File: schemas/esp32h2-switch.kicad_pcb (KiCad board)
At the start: 2 copper layers, 81.3 x 58.4 mm, 21 parts, among them J1 Screw_Terminal_01x02, J2 Screw_Terminal_01x02, J3 Conn_01x15, J4 Conn_01x15, K1 SPDT, 5V 72R, 10A 250VAC, Q1 NPN, 40V, 500mA, U1 LM1117MP-3.3

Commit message: Fix nets due to checks
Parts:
- turned F1 to 0 degrees
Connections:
- F1 pad 1: L -> L_IN
- F1 pad 2: L -> /L
- J1 pad 1: L -> L_IN
- J2 pad 1: L -> /L_OUT
- K1 pad 11: L -> L_IN
- K1 pad 14: L -> /L_OUT
- PS1 pad 1: L -> /L
- RV1 pad 1: L -> /L
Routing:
- net L: track 73.9 -> 0.00 mm
- net L_IN: track 0.00 -> 40.1 mm
- net /L_OUT: track 0.00 -> 17.3 mm
- net /L: track 0.00 -> 16.5 mm
- net Net-(J3-Pin_9): track 66.8 -> 67.3 mm
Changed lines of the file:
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@@
 	(net 5 "/RELAY_COIL")
 	(net 6 "/LED_RELAY")
-	(net 7 "L")
+	(net 7 "L_IN")
 	(net 8 "unconnected-(J3-Pin_8-Pad8)")
 	(net 9 "/RELAY_CTRL")
@@
 	(net 37 "Net-(Q1-B)")
 	(net 38 "N")
+	(net 39 "/L")
+	(net 40 "/L_OUT")
 	(footprint "TerminalBlock_Phoenix:TerminalBlock_Phoenix_MKDS-1,5-2-5.08_1x02_P5.08mm_Horizontal"
 		(layer "F.Cu")
@@
 			(remove_unused_layers no)
 			(roundrect_rratio 0.096154)
-			(net 7 "L")
+			(net 40 "/L_OUT")
 			(pinfunction "Pin_1")
 			(pintype "passive")
@@
 			(layers "*.Cu" "*.Mask")
 			(remove_unused_layers no)
-			(net 7 "L")
+			(net 39 "/L")
 			(pinfunction "AC/L")
 			(pintype "power_in")
@@
 			(remove_unused_layers no)
 			(roundrect_rratio 0.096154)
-			(net 7 "L")
+			(net 7 "L_IN")
 			(pinfunction "Pin_1")
 			(pintype "passive")
@@
 		(tags "LED")
 		(property "Reference" "D1"
-			(at -0.635 -1.987701 180)
+			(at -0.635 -2.54 180)
 			(layer "F.SilkS")
 			(effects
@@
 	(footprint "Sivakov_FuseHolders_THT:FuseHolder_THT_5x20mm_PTF76_RM15mm"
 		(layer "F.Cu")
-		(at 57.15 62.23 180)
+		(at 57.15 62.23)
 		(property "Reference" "F1"
 			(at 0 0 0)
@@
 		(attr through_hole)
 		(fp_line
-			(start 12.3 4.8)
-			(end -12.3 4.8)
+			(start -12.3 -4.8)
+			(end 12.3 -4.8)
 			(stroke
 				(width 0.2)
@@
 		)
 		(fp_line
-			(start 12.3 -4.8)
-			(end 12.3 4.8)
+			(start -12.3 4.8)
+			(end -12.3 -4.8)
 			(stroke
 				(width 0.2)
@@
 		)
 		(fp_line
-			(start -12.3 4.8)
-			(end -12.3 -4.8)
+			(start 12.3 -4.8)
+			(end 12.3 4.8)
 			(stroke
 				(width 0.2)
@@
 		)
 		(fp_line
-			(start -12.3 -4.8)
-			(end 12.3 -4.8)
+			(start 12.3 4.8)
+			(end -12.3 4.8)
 			(stroke
 				(width 0.2)
@@
 		)
 		(fp_line
-			(start 12.5 5)
-			(end -12.5 5)
+			(start -12.5 -5)
+			(end 12.5 -5)
 			(stroke
 				(width 0.05)
-				(type default)
+				(type solid)
 			)
 			(layer "F.CrtYd")
 		)
 		(fp_line
-			(start 12.5 -5)
-			(end 12.5 5)
+			(start -12.5 5)
+			(end -12.5 -5)
 			(stroke
 				(width 0.05)
@@
 		)
 		(fp_line
-			(start -12.5 5)
-			(end -12.5 -5)
+			(start 12.5 -5)
+			(end 12.5 5)
 			(stroke
 				(width 0.05)
@@
 		)
 		(fp_line
-			(start -12.5 -5)
-			(end 12.5 -5)
+			(start 12.5 5)
+			(end -12.5 5)
 			(stroke
 				(width 0.05)
-				(type solid)
+				(type default)
 			)
 			(layer "F.CrtYd")
 		)
 		(fp_line
-			(start 12.2 4.7)
-			(end -12.2 4.7)
+			(start -12.2 -4.7)
+			(end 12.2 -4.7)
 			(stroke
 				(width 0.1)
@@
 		)
 		(fp_line
-			(start 12.2 -4.7)
-			(end 12.2 4.7)
+			(start -12.2 4.7)
+			(end -12.2 -4.7)
 			(stroke
 				(width 0.1)
@@
 		)
 		(fp_line
-			(start -12.2 4.7)
-			(end -12.2 -4.7)
+			(start 12.2 -4.7)
+			(end 12.2 4.7)
 			(stroke
 				(width 0.1)
@@
 		)
 		(fp_line
-			(start -12.2 -4.7)
-			(end 12.2 -4.7)
+			(start 12.2 4.7)
+			(end -12.2 4.7)
 			(stroke
 				(width 0.1)
@@
 		)
 		(pad "1" thru_hole circle
-			(at -7.5 0 180)
+			(at -7.5 0)
 			(size 2.5 2.5)
 			(drill 1.5)
 			(layers "*.Cu" "*.Mask")
 			(remove_unused_layers no)
-			(net 7 "L")
+			(net 7 "L_IN")
 			(pintype "passive")
 			(solder_mask_margin 0.102)
 		)
 		(pad "2" thru_hole circle
-			(at 7.5 0 180)
+			(at 7.5 0)
 			(size 2.25 2.25)
 			(drill 1.5)
 			(layers "*.Cu" "*.Mask")
 			(remove_unused_layers no)
-			(net 7 "L")
+			(net 39 "/L")
 			(pintype "passive")
 			(solder_mask_margin 0.102)
@@
 			(layers "*.Cu" "*.Mask")
 			(remove_unused_layers no)
-			(net 7 "L")
+			(net 39 "/L")
 			(pintype "passive")
 		)
@@
 		(tags "LED")
 		(property "Reference" "D3"
-			(at -0.635 -1.905 180)
+			(at -0.635 -2.54 180)
 			(layer "F.SilkS")
 			(effects
@@
 			(layers "*.Cu" "*.Mask")
 			(remove_unused_layers no)
-			(net 7 "L")
+			(net 7 "L_IN")
 			(pintype "passive")
 		)
@@
 			(layers "*.Cu" "*.Mask")
 			(remove_unused_layers no)
-			(net 7 "L")
+			(net 40 "/L_OUT")
 			(pintype "passive")
 		)
@@
 	)
 	(segment
-		(start 42.476571 73.66)
-		(end 47.86 79.043429)
-		(width 3)
-		(layer "B.Cu")
-		(net 7)
-	)
-	(segment
-		(start 57.277142 62.23)
-		(end 64.869 69.821858)
-		(width 3)
-		(layer "B.Cu")
-		(net 7)
-	)
-	(segment
-		(start 76.708 67.564)
-		(end 73.152 67.564)
-		(width 3)
-		(layer "B.Cu")
-		(net 7)
-	)
-	(segment
-		(start 47.86 79.043429)
-		(end 47.86 84.3245)
-		(width 3)
-		(layer "B.Cu")
-		(net 7)
-	)
-	(segment
-		(start 49.65 62.23)
-		(end 57.277142 62.23)
-		(width 3)
-		(layer "B.Cu")
-		(net 7)
-	)
-	(segment
 		(start 38.1 60.96)
 		(end 48.38 60.96)
@@
 	)
 	(segment
-		(start 73.152 67.564)
-		(end 71.12 69.596)
-		(width 3)
-		(layer "B.Cu")
-		(net 7)
-	)
-	(segment
-		(start 64.65 63.126)
-		(end 71.12 69.596)
-		(width 3)
-		(layer "B.Cu")
-		(net 7)
-	)
-	(segment
-		(start 64.869 69.821858)
-		(end 64.869 75.5155)
+		(start 64.811 75.5735)
+		(end 62.06 78.3245)
 		(width 3)
 		(layer "B.Cu")
@@
 	)
 	(segment
-		(start 64.65 62.23)
-		(end 64.65 63.126)
+		(start 49.65 62.23)
+		(end 57.277142 62.23)
 		(width 3)
 		(layer "B.Cu")
@@
 	)
 	(segment
-		(start 64.869 75.5155)
-		(end 62.06 78.3245)
+		(start 57.277142 62.23)
+		(end 64.811 69.763858)
 		(width 3)
 		(layer "B.Cu")
@@
 	)
 	(segment
-		(start 38.1 73.66)
-		(end 42.476571 73.66)
+		(start 64.811 69.763858)
+		(end 64.811 75.5735)
 		(width 3)
 		(layer "B.Cu")
@@
 	)
 	(segment
-		(start 65.914 113.156)
-		(end 88.9 90.17)
+		(start 42.545 109.22)
+		(end 46.99 113.665)
 		(width 0.25)
 		(layer "F.Cu")
@@
 	)
 	(segment
-		(start 42.545 109.22)
-		(end 46.481 113.156)
+		(start 65.405 113.665)
+		(end 88.9 90.17)
 		(width 0.25)
 		(layer "F.Cu")
@@
 	)
 	(segment
-		(start 46.481 113.156)
-		(end 65.914 113.156)
+		(start 46.99 113.665)
+		(end 65.405 113.665)
 		(width 0.25)
 		(layer "F.Cu")
@@
 	)
 	(segment
-		(start 36.195 109.22)
-		(end 40.582 113.607)
+		(start 41.275 114.3)
+		(end 67.31 114.3)
 		(width 0.25)
 		(layer "F.Cu")
@@
 	)
 	(segment
-		(start 40.582 113.607)
-		(end 68.003 113.607)
+		(start 67.31 114.3)
+		(end 91.44 90.17)
 		(width 0.25)
 		(layer "F.Cu")
@@
 	)
 	(segment
-		(start 68.003 113.607)
-		(end 91.44 90.17)
+		(start 36.195 109.22)
+		(end 41.275 114.3)
 		(width 0.25)
 		(layer "F.Cu")
@@
 		(net 38)
 	)
+	(segment
+		(start 64.65 62.23)
+		(end 64.65 63.126)
+		(width 3)
+		(layer "B.Cu")
+		(net 39)
+	)
+	(segment
+		(start 76.708 67.564)
+		(end 73.152 67.564)
+		(width 3)
+		(layer "B.Cu")
+		(net 39)
+	)
+	(segment
+		(start 64.65 63.126)
+		(end 71.12 69.596)
+		(width 3)
+		(layer "B.Cu")
+		(net 39)
+	)
+	(segment
+		(start 73.152 67.564)
+		(end 71.12 69.596)
+		(width 3)
+		(layer "B.Cu")
+		(net 39)
+	)
+	(segment
+		(start 42.476571 73.66)
+		(end 47.86 79.043429)
+		(width 3)
+		(layer "B.Cu")
+		(net 40)
+	)
+	(segment
+		(start 47.86 79.043429)
+		(end 47.86 84.3245)
+		(width 3)
+		(layer "B.Cu")
+		(net 40)
+	)
+	(segment
+		(start 38.1 73.66)
+		(end 42.476571 73.66)
+		(width 3)
+		(layer "B.Cu")
+		(net 40)
+	)
 	(zone
 		(net 3)
@@
 		(polygon
 			(pts
-				(xy 51.435 107.315) (xy 59.055 107.315) (xy 59.055 113.03) (xy 51.435 113.03)
-			)
-		)
-	)
-	(zone
-		(net 0)
-		(net_name "")
-		(layer "F.Cu")
-		(hatch edge 0.5)
-		(connect_pads yes
-			(clearance 0)
-		)
-		(min_thickness 0.25)
-		(filled_areas_thickness no)
-		(keepout
-			(tracks not_allowed)
-			(vias not_allowed)
-			(pads allowed)
-			(copperpour allowed)
-			(footprints allowed)
-		)
-		(placement
-			(enabled no)
-			(sheetname "/")
-		)
-		(fill
-			(thermal_gap 0.5)
-			(thermal_bridge_width 0.5)
-		)
-		(polygon
-			(pts
-				(xy 51.435 107.315) (xy 59.055 107.315) (xy 59.055 113.03) (xy 51.435 113.03)
+				(xy 51.435 106.045) (xy 59.055 106.045) (xy 59.055 113.03) (xy 51.435 113.03)
 			)
 		)

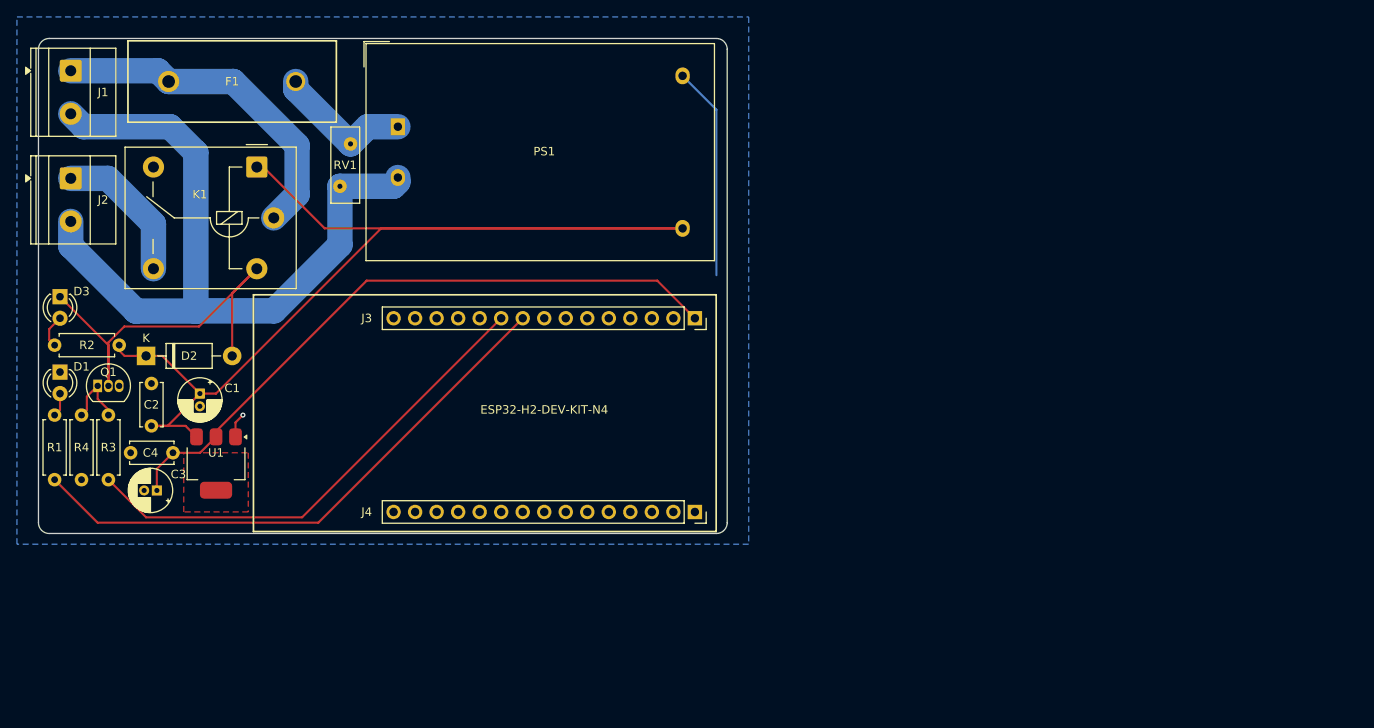
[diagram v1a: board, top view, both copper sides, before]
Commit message: Better arragement components + more copper fields
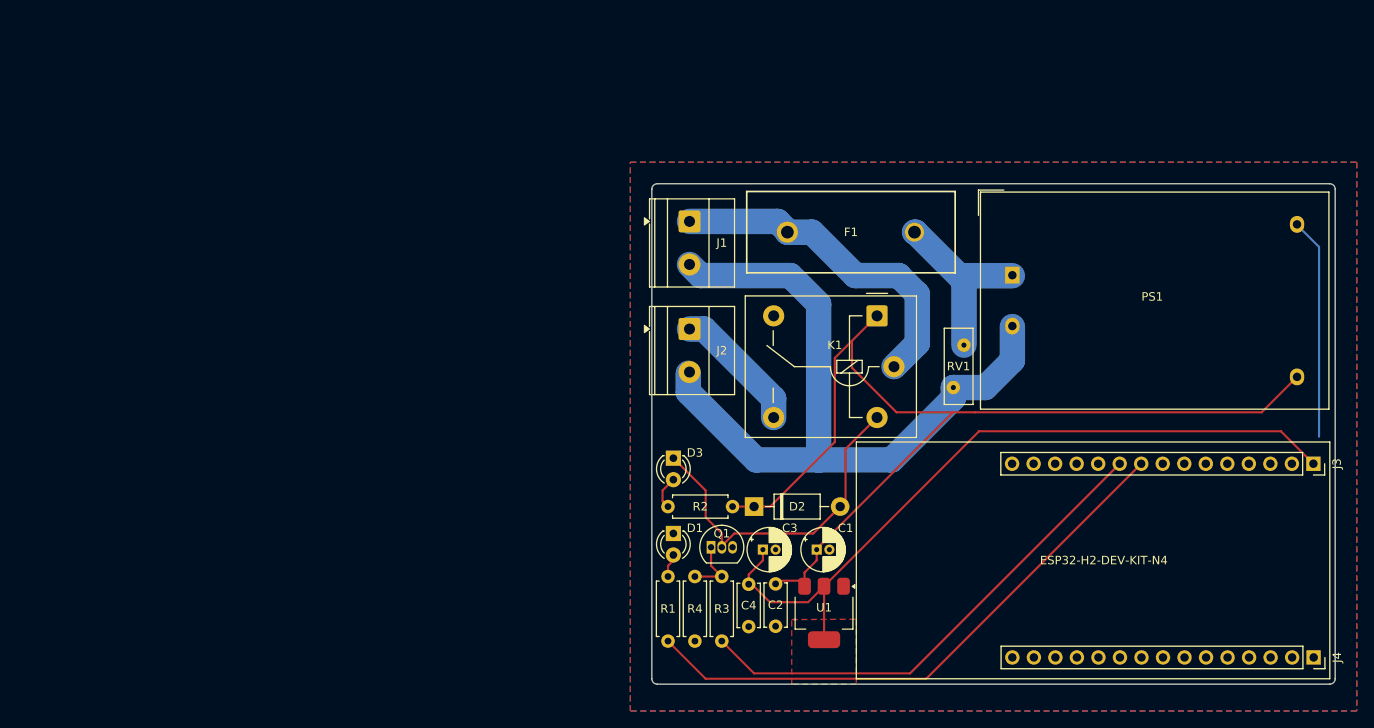
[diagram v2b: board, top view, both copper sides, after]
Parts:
- moved RV1 76.2 mm to (143.5, 93.3)
- moved C2 76.0 mm to (121.3, 121.5), turned to -90 degrees
- moved K1 75.3 mm to (135.3, 95.9)
- moved F1 75.2 mm to (130.2, 80.0)
- moved J1 75.2 mm to (111.1, 78.7)
- moved J2 75.2 mm to (111.1, 91.4)
- moved C1 75.1 mm to (126.1, 117.5), turned to 0 degrees
- moved J4 75.0 mm to (184.8, 130.2)
- moved J3 75.0 mm to (184.8, 107.3)
- moved Q1 74.9 mm to (113.7, 117.2)
- moved R4 74.9 mm to (111.8, 120.7)
- moved D1 74.9 mm to (109.2, 115.6)
- moved D3 74.9 mm to (109.2, 106.7)
- moved R2 74.9 mm to (116.2, 112.4)
- moved R3 74.9 mm to (114.9, 128.3)
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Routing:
- net +5V: track 144.8 -> 125.2 mm
- net +3.3V: track 78.1 -> 88.5 mm
- net /RELAY_COIL: track 50.6 -> 42.0 mm
- net /L: track 16.5 -> 21.8 mm
- net GND: track 28.1 -> 26.1 mm, vias 1 -> 0
- net N: track 90.9 -> 89.0 mm
- net /L_OUT: track 17.3 -> 15.6 mm
- net Net-(Q1-B): track 8.22 -> 7.15 mm
- net Net-(J3-Pin_9): track 67.3 -> 68.2 mm
- net /RELAY_CTRL: track 57.9 -> 58.8 mm
- added copper zone on F.Cu, net GND
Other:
- board size 81.3 x 58.4 mm -> 80.6 x 59.1 mm

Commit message: Better layout for hand soldering
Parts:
- Q1: footprint Package_TO_SOT_THT:TO-92_Inline -> Package_TO_SOT_THT:TO-92_Inline_Wide
- moved C3 1.55 mm to (121.3, 117.1)
- moved C1 0.95 mm to (127.0, 117.1)
- moved Q1 0.64 mm to (113.0, 117.2)
- moved U1 0.49 mm to (127.0, 124.5)
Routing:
- net +5V: track 125.2 -> 119.3 mm
- net +3.3V: track 88.5 -> 90.6 mm
- net /RELAY_COIL: track 42.0 -> 40.8 mm
- net GND: track 26.1 -> 25.2 mm
- net /LED_RELAY: track 3.96 -> 3.44 mm
